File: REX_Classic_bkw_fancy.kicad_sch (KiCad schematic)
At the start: 12 parts, among them J1 Tandy_100_102_200_option_rom, J2 JTAG, J3 PRG, U1 XCR3064XL-VQ44, U2 29F800BB, U3 LP2980-3.3

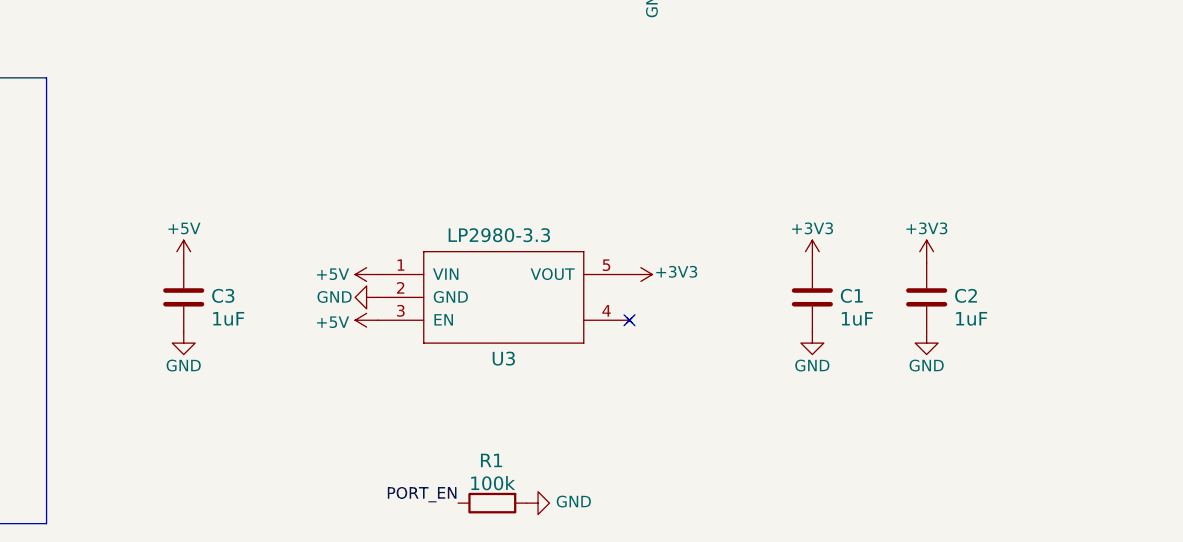
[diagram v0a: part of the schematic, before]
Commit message: kicad 7, 0.2mm tracks, 0.3x0.5mm vias, add caps on 3v3
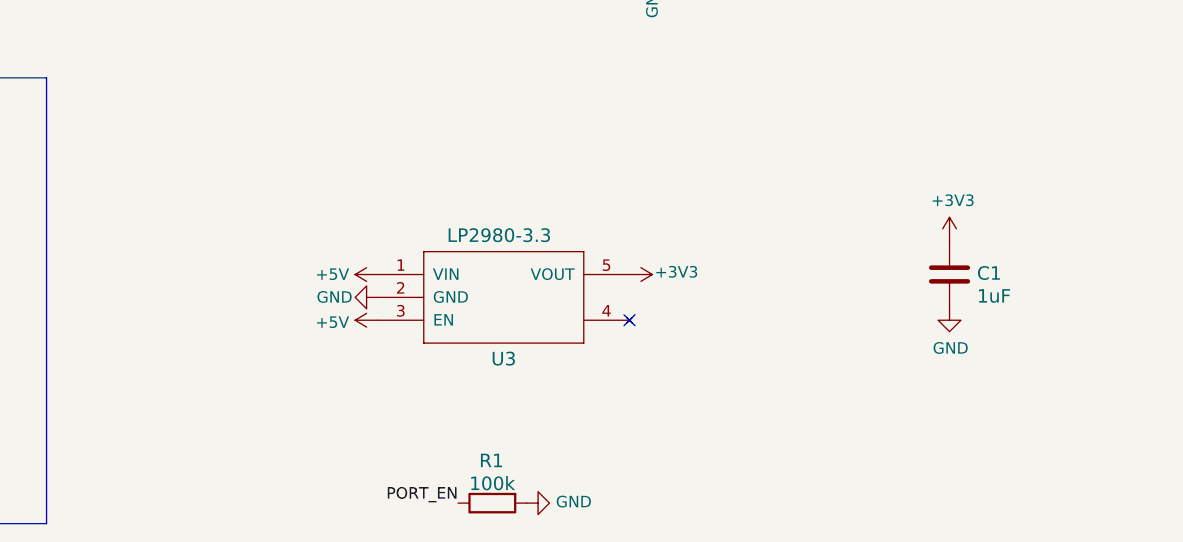
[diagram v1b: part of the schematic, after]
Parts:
- removed C2, C3: 1uF, 000_LOCAL:C_0805, symbol 000_LOCAL:C
- J1: footprint 000_LOCAL:Molex78802_PCB_28_REX -> 000_LOCAL:Molex78802_PCB_28_REX_slots
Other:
- company: Brian K. White - b.kenyon.w@gmail.com -> (none)
- title: REX Classic bkw -> (none)
- moved on the sheet: C1
